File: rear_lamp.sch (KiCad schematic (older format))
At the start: 9 parts, among them J1 PWR, Q1 BD137

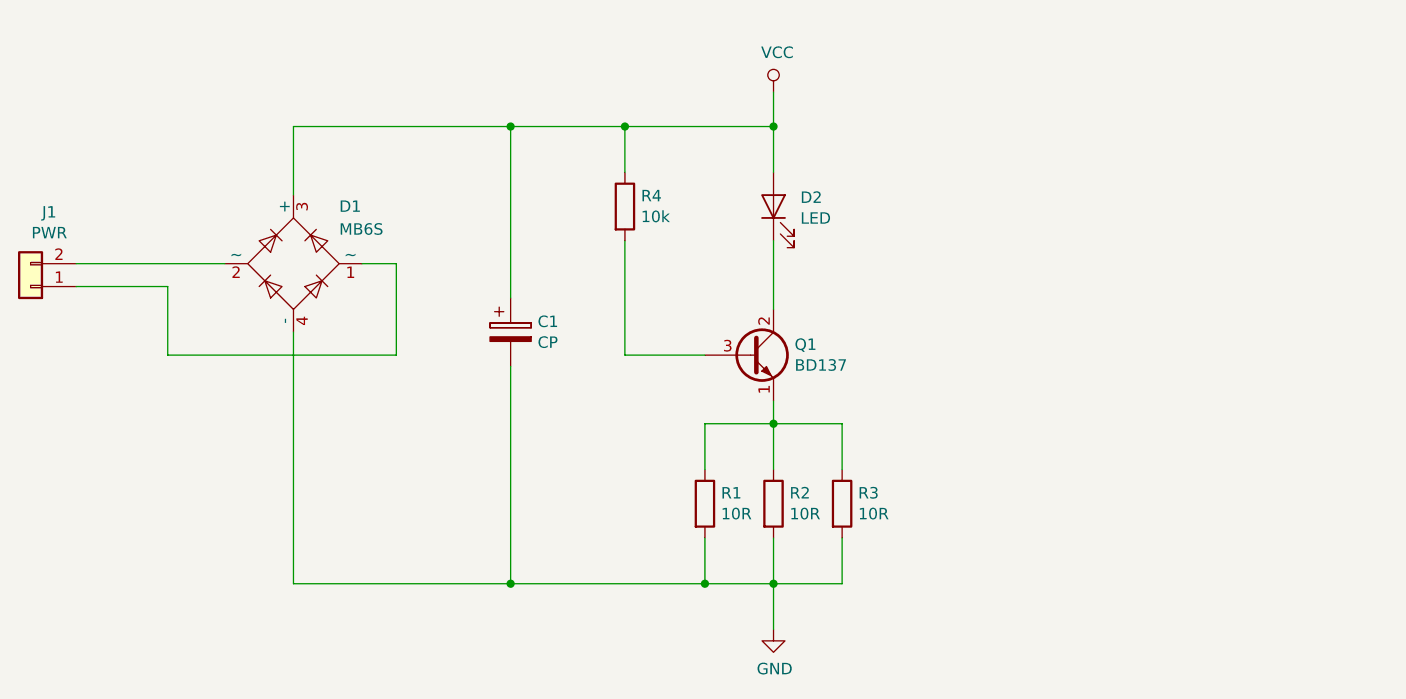
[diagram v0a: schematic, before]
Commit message: discrete led driver
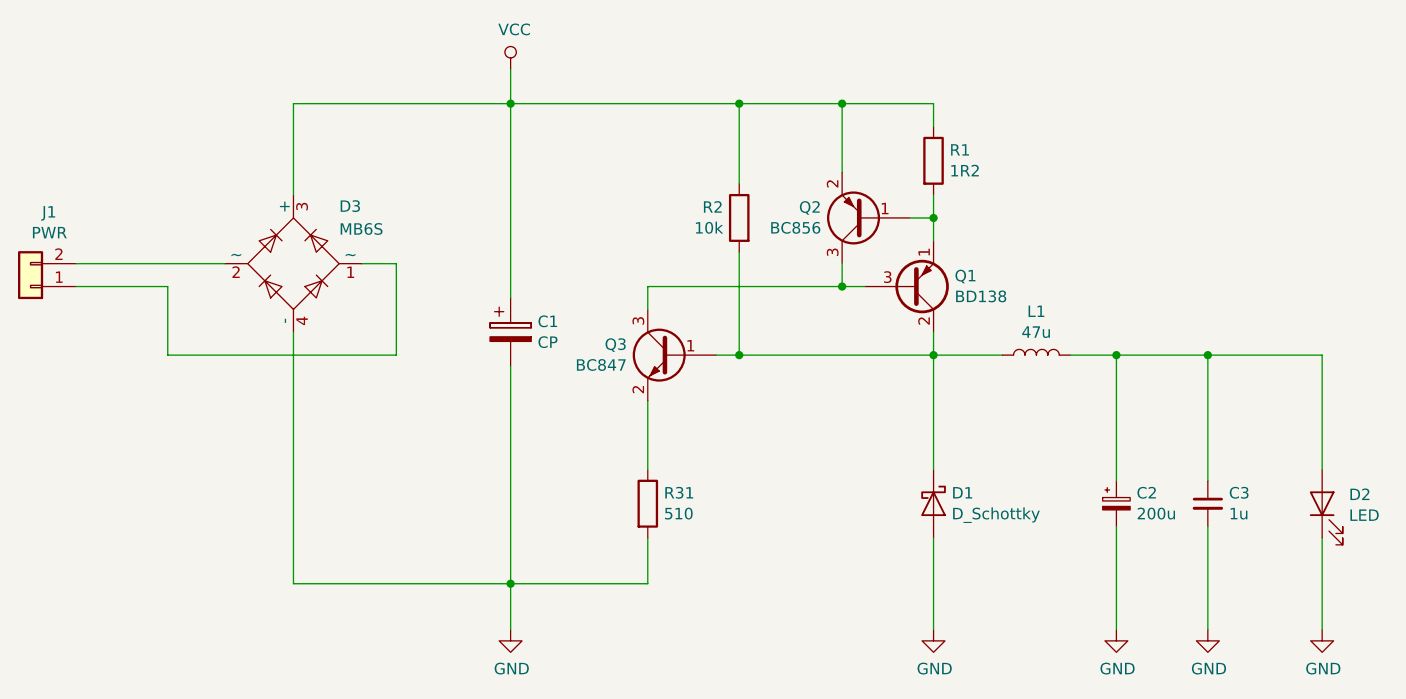
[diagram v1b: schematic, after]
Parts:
- removed Q1: BD137, Package_TO_SOT_THT:TO-126-3_Vertical, symbol Transistor_BJT:BD137
- removed R3: 10R, Resistor_SMD:R_0805_2012Metric_Pad1.15x1.40mm_HandSolder, symbol Device:R
- removed R4: 10k, Resistor_SMD:R_0805_2012Metric_Pad1.15x1.40mm_HandSolder, symbol Device:R
- added C2: 200u, Capacitor_THT:CP_Radial_D8.0mm_P3.80mm, symbol Device:CP_Small
- added C3: 1u, Capacitor_SMD:C_0805_2012Metric_Pad1.15x1.40mm_HandSolder, symbol Device:C_Small
- added D1: D_Schottky, Diode_SMD:D_SOD-123, symbol Device:D_Schottky
- added L1: 47u, Inductor_SMD:L_Coilcraft_XAL60xx_6.36x6.56mm, symbol Device:L
- added Q1: BD138, Package_TO_SOT_THT:TO-126-3_Vertical, symbol Transistor_BJT:BD138
- added Q2: BC856, Package_TO_SOT_SMD:SOT-23, symbol Transistor_BJT:BC856
- added Q3: BC847, Package_TO_SOT_SMD:SOT-23, symbol Transistor_BJT:BC847
- added R1: 1R2, Resistor_SMD:R_1206_3216Metric_Pad1.42x1.75mm_HandSolder, symbol Device:R
- R2: value 10R -> 10k
- R31: renamed from R1; value 10R -> 510
- renumbered D1 to D3
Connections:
- net GND: now also D2.1 (K), C2.2, C3.2, D1.2 (A); no longer R2.2
- net VCC: now also R2.1, Q2.2 (E), R1.1; no longer D2.2 (A)
- net at R31.1: now also Q3.2 (E); no longer R2.1
- new net: C2.1, C3.1, D2.2 (A), L1.2
- new net: Q1.1 (E), Q2.1 (B), R1.2
- new net: Q1.3 (B), Q2.3 (C), Q3.3 (C)
- new net: D1.1 (K), L1.1, Q1.2 (C), Q3.1 (B), R2.2
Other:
- moved on the sheet: D2, R31

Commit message: one plane
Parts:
- removed D3: MB6S, Package_TO_SOT_SMD:TO-269AA, symbol Diode_Bridge:MB6S
- C1: footprint Capacitor_THT:CP_Radial_D10.0mm_P5.00mm -> Capacitor_THT:C_Axial_L5.1mm_D3.1mm_P12.50mm_Horizontal
- D1: footprint Diode_SMD:D_SOD-123 -> Diode_SMD:D_SMA_Handsoldering
- L1: footprint Inductor_SMD:L_Coilcraft_XAL60xx_6.36x6.56mm -> Inductor_SMD:L_Bourns_SRP7028A_7.3x6.6mm
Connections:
- net GND: now also J1.1 (Pin_1)
- net VCC: now also J1.2 (Pin_2)
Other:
- moved on the sheet: J1
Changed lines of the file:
@@
-$EndComp
-$Comp
-L Diode_Bridge:MB6S D3
-U 1 1 65E9DBBF
-P 2700 2800
-F 0 "D3" V 2950 2600 50  0000 R CNN
-F 1 "MB6S" V 2850 2600 50  0000 R CNN
-F 2 "Package_TO_SOT_SMD:TO-269AA" H 2850 2925 50  0001 L CNN
-F 3 "http://www.vishay.com/docs/88573/dfs.pdf" H 2700 2800 50  0001 C CNN
-	1    2700 2800
-	0    -1   -1   0
 $EndComp
 $Comp
@@
 	3650 2100 3650 1950
 Wire Wire Line
-	2700 3100 2700 4200
-Wire Wire Line
-	2700 4200 3650 4200
-Wire Wire Line
 	4250 4200 4250 4000
 $Comp
@@
 F 0 "C1" H 3768 3146 50  0000 L CNN
 F 1 "CP" H 3768 3055 50  0000 L CNN
-F 2 "Capacitor_THT:CP_Radial_D10.0mm_P5.00mm" H 3688 2950 50  0001 C CNN
+F 2 "Capacitor_THT:C_Axial_L5.1mm_D3.1mm_P12.50mm_Horizontal" H 3688 2950 50  0001 C CNN
 F 3 "~" H 3650 3100 50  0001 C CNN
 	1    3650 3100
@@
 L Connector_Generic:Conn_01x02 J1
 U 1 1 65F3A3FF
-P 1550 2900
-F 0 "J1" H 1468 2575 50  0000 C CNN
-F 1 "PWR" H 1468 2666 50  0000 C CNN
-F 2 "Connector_Wire:SolderWirePad_1x02_P3.81mm_Drill1mm" H 1550 2900 50  0001 C CNN
-F 3 "~" H 1550 2900 50  0001 C CNN
-	1    1550 2900
+P 2850 3150
+F 0 "J1" H 2768 2825 50  0000 C CNN
+F 1 "PWR" H 2768 2916 50  0000 C CNN
+F 2 "Connector_Wire:SolderWirePad_1x02_P3.81mm_Drill1mm" H 2850 3150 50  0001 C CNN
+F 3 "~" H 2850 3150 50  0001 C CNN
+	1    2850 3150
 	-1   0    0    1
 $EndComp
 Wire Wire Line
-	2400 2800 1750 2800
-Wire Wire Line
-	2150 3200 3150 3200
-Wire Wire Line
-	3150 3200 3150 2800
-Wire Wire Line
-	3150 2800 3000 2800
-Wire Wire Line
-	1750 2900 2150 2900
-Wire Wire Line
-	2150 2900 2150 3200
+	3050 3150 3450 3150
 $Comp
 L Device:R R31
@@
 Wire Wire Line
 	5500 2100 5500 2200
-Wire Wire Line
-	3650 2100 2700 2100
 Connection ~ 3650 2100
-Wire Wire Line
-	2700 2100 2700 2500
 Wire Wire Line
 	3650 2100 3650 2950
@@
 F 0 "L1" V 6140 3200 50  0000 C CNN
 F 1 "47u" V 6049 3200 50  0000 C CNN
-F 2 "Inductor_SMD:L_Coilcraft_XAL60xx_6.36x6.56mm" H 5950 3200 50  0001 C CNN
+F 2 "Inductor_SMD:L_Bourns_SRP7028A_7.3x6.6mm" H 5950 3200 50  0001 C CNN
 F 3 "~" H 5950 3200 50  0001 C CNN
 	1    5950 3200
@@
 F 0 "D1" V 5454 3929 50  0000 L CNN
 F 1 "D_Schottky" V 5545 3929 50  0000 L CNN
-F 2 "Diode_SMD:D_SOD-123" H 5500 3850 50  0001 C CNN
+F 2 "Diode_SMD:D_SMA_Handsoldering" H 5500 3850 50  0001 C CNN
 F 3 "~" H 5500 3850 50  0001 C CNN
 	1    5500 3850
@@
 Wire Wire Line
 	7200 4000 7200 4400
+Wire Wire Line
+	3050 3050 3450 3050
+Wire Wire Line
+	3450 2100 3650 2100
+Wire Wire Line
+	3450 2100 3450 3050
+Wire Wire Line
+	3450 4200 3650 4200
+Wire Wire Line
+	3450 3150 3450 4200
 $EndSCHEMATC

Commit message: small pcb
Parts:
- D2: footprint LED_THT:LED_D3.0mm -> Capacitor_THT:C_Axial_L5.1mm_D3.1mm_P12.50mm_Horizontal
- renumbered R31 to R3
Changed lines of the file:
@@
 EESchema Schematic File Version 4
-EELAYER 30 0
+LIBS:rear_lamp-cache
+EELAYER 26 0
 EELAYER END
 $Descr A4 11693 8268
@@
 F 0 "D2" V 7239 3733 50  0000 R CNN
 F 1 "LED" V 7148 3733 50  0000 R CNN
-F 2 "LED_THT:LED_D3.0mm" H 7200 3850 50  0001 C CNN
+F 2 "Capacitor_THT:C_Axial_L5.1mm_D3.1mm_P12.50mm_Horizontal" H 7200 3850 50  0001 C CNN
 F 3 "~" H 7200 3850 50  0001 C CNN
 	1    7200 3850
@@
 	3050 3150 3450 3150
 $Comp
-L Device:R R31
+L Device:R R3
 U 1 1 65F3697B
 P 4250 3850
-F 0 "R31" H 4320 3896 50  0000 L CNN
+F 0 "R3" H 4320 3896 50  0000 L CNN
 F 1 "510" H 4320 3805 50  0000 L CNN
 F 2 "Resistor_SMD:R_0805_2012Metric_Pad1.15x1.40mm_HandSolder" V 4180 3850 50  0001 C CNN
